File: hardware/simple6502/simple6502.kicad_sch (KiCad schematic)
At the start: 19 parts, among them J1 ~{VP}, J2 CLK SEL, J3 RESET, SW1 RESET, T1 DS1813-10+, U1 W65C02SxP, U2 RAM 62256, U3 ROM 28C256, U4 74LS30, U5 74HCT00, U6 74HC138, X1 ACO-1MHz

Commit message: All in One PCB  v1.1
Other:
- title: simple6502 -> All in One - simple6502
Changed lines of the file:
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@@
   (paper "USLetter")
   (title_block
-    (title "simple6502")
+    (title "All in One - simple6502")
     (date "2023-10-01")
     (rev "1.1")

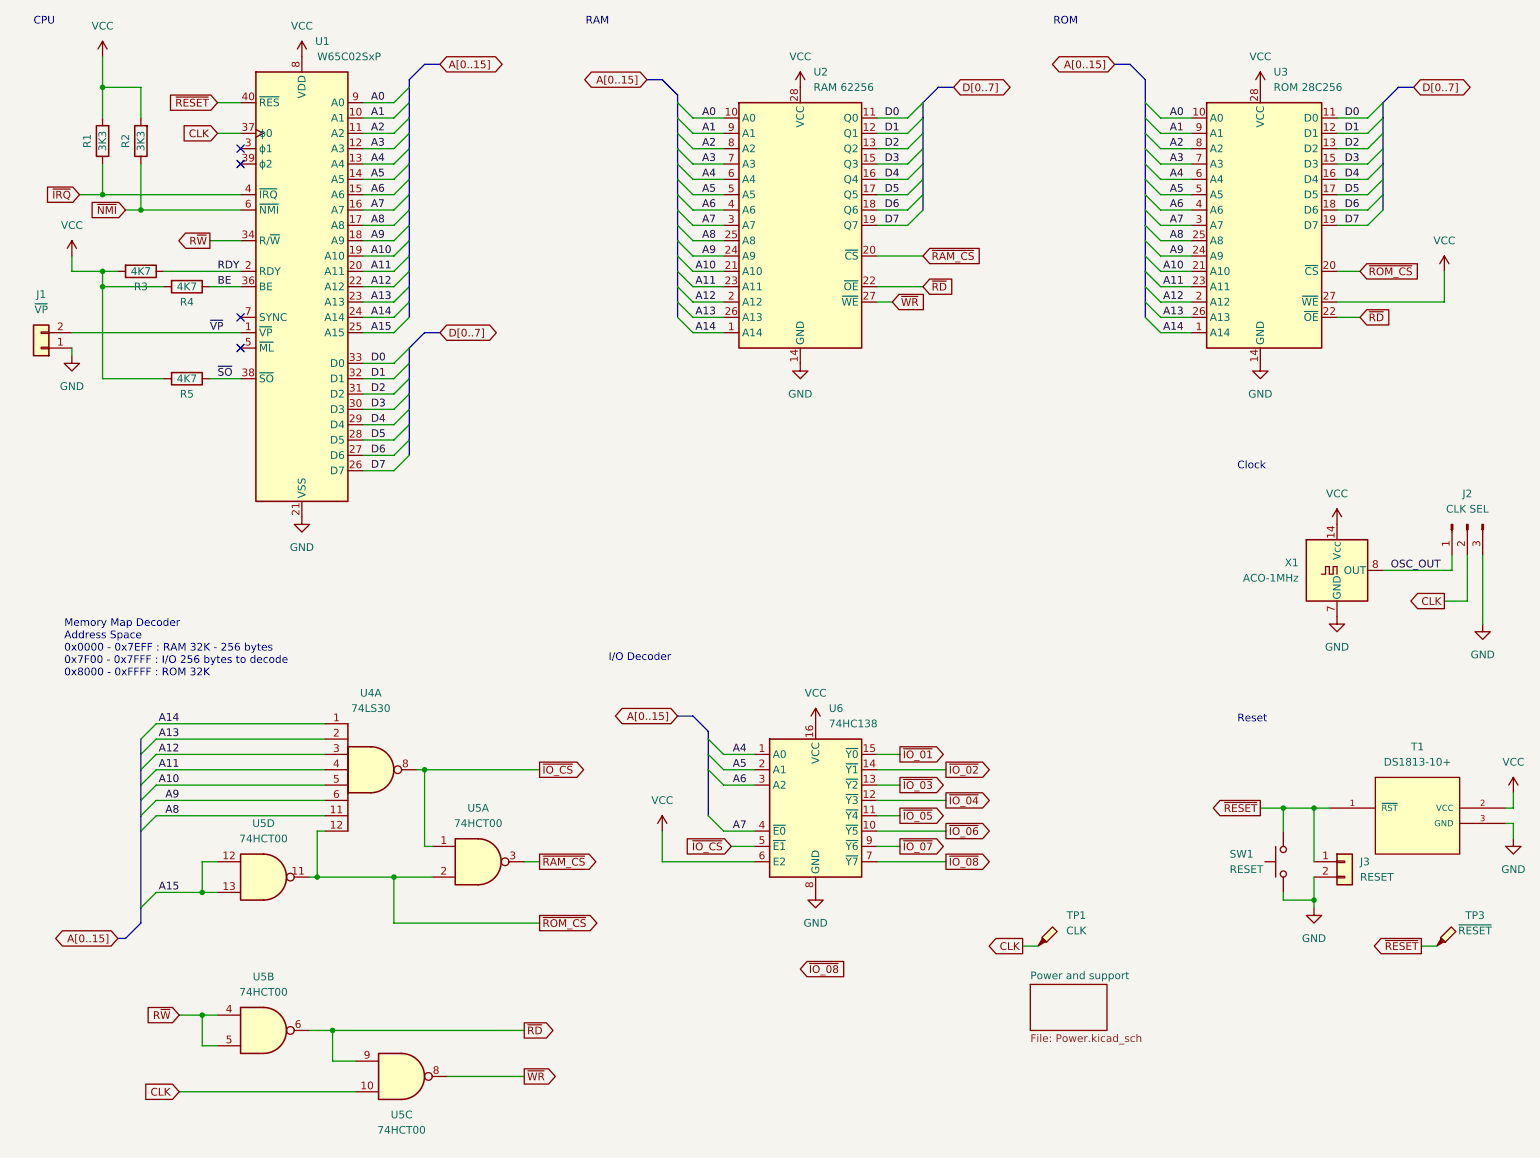
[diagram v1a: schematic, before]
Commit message: new all in one design with ACIA 68B50
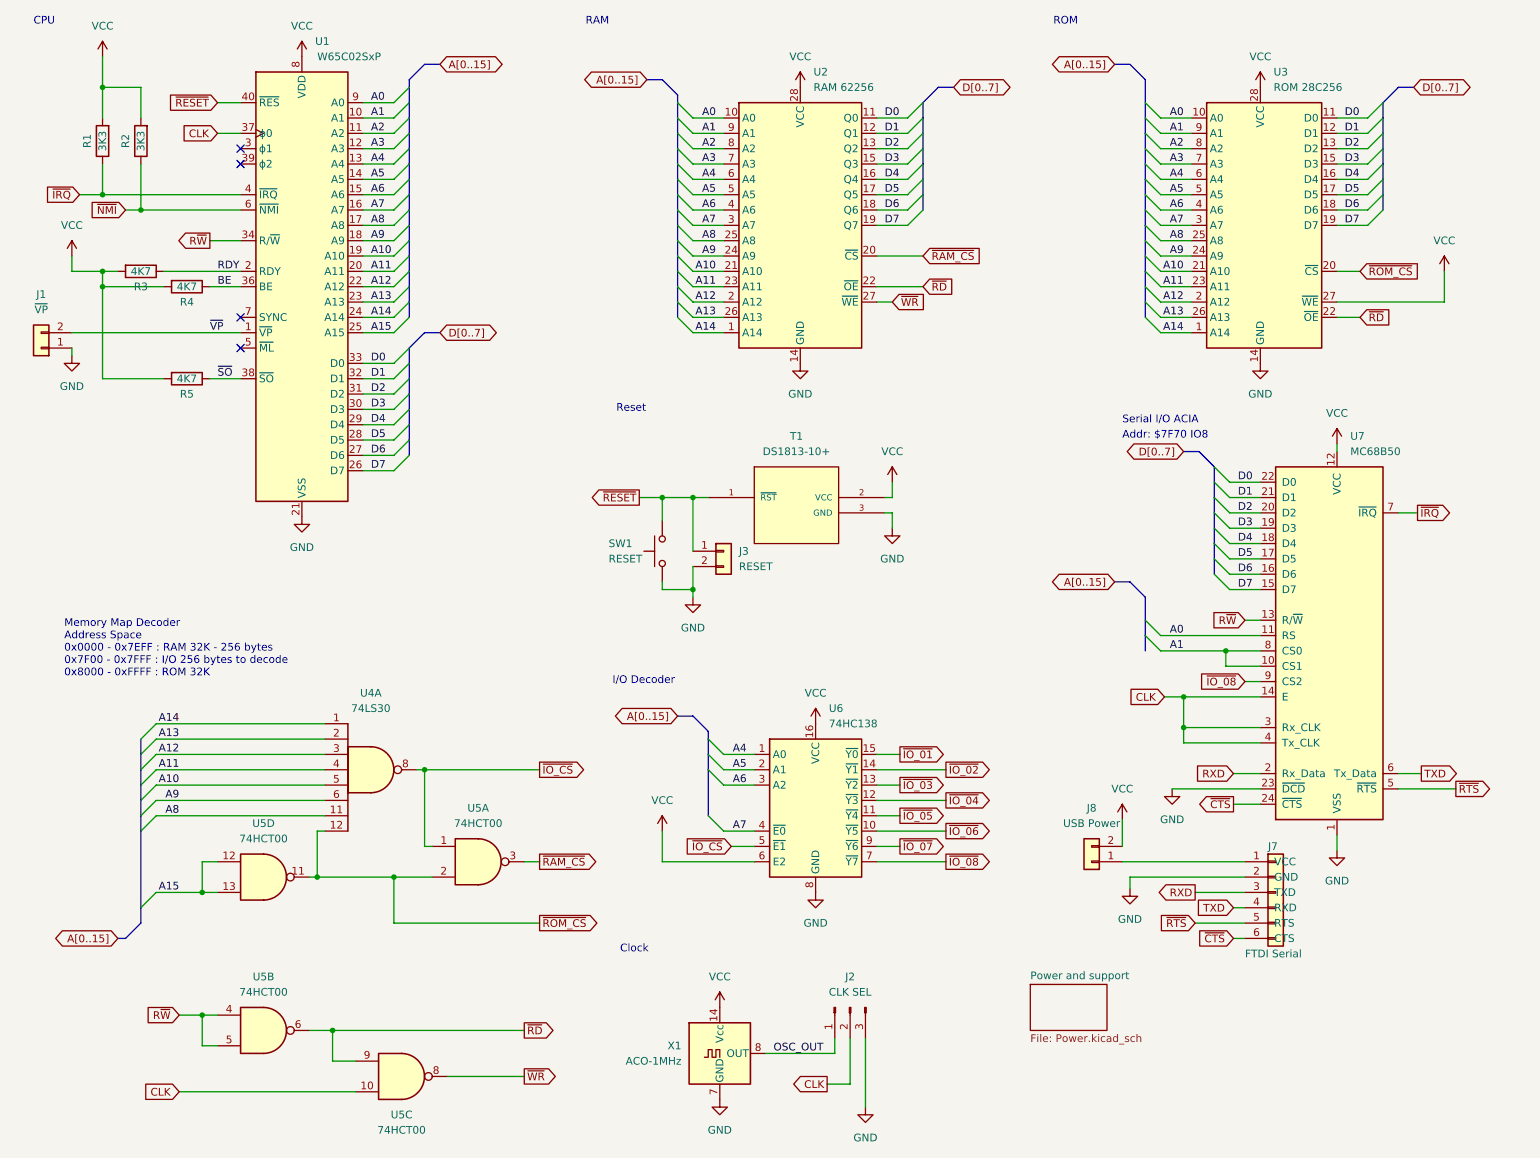
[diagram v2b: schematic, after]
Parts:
- removed TP1: CLK, TestPoint:TestPoint_THTPad_2.0x2.0mm_Drill1.0mm, symbol Connector:TestPoint_Probe
- removed TP3: ~{RESET}, TestPoint:TestPoint_THTPad_1.5x1.5mm_Drill0.7mm, symbol Connector:TestPoint_Probe
- added J7: FTDI Serial, Connector_PinSocket_2.54mm:PinSocket_1x06_P2.54mm_Vertical, symbol Connector_Generic:Conn_01x06
- added J8: USB Power, Connector_PinHeader_2.54mm:PinHeader_1x02_P2.54mm_Vertical, symbol Connector_Generic:Conn_01x02
- added U7: MC68B50, Package_DIP:DIP-24_W15.24mm_Socket, symbol Interface_UART:MC68B50
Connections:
- net A0: now also U7.11 (RS)
- net A1: now also U7.10 (CS1), U7.8 (CS0)
- net CLK: now also U7.14 (E), U7.3 (Rx_CLK), U7.4 (Tx_CLK)
- net D0: now also U7.22 (D0)
- net D1: now also U7.21 (D1)
- net D2: now also U7.20 (D2)
- net D3: now also U7.19 (D3)
- net D4: now also U7.18 (D4)
- net D5: now also U7.17 (D5)
- net D6: now also U7.16 (D6)
- net D7: now also U7.15 (D7)
- net GND: now also J7.2 (GND), U7.1 (VSS), U7.23 (~{DCD})
- net R~{W}: now also U7.13 (R/~{W})
- net VCC: now also J8.2 (Pin_2), U7.12 (VCC)
- net ~{IO_08}: now also U7.9 (CS2)
- net ~{IRQ}: now also U7.7 (~{IRQ})
- new net: J7.1 (VCC), J8.1 (Pin_1)
- new net RXD: J7.3 (TXD), U7.2 (Rx_Data)
- new net TXD: J7.4 (RXD), U7.6 (Tx_Data)
- new net ~{CTS}: J7.6 (CTS), U7.24 (~{CTS})
- new net ~{RTS}: J7.5 (RTS), U7.5 (~{RTS})
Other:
- note added: "Addr: $7F70 IO8"
- note added: "Serial I/O ACIA"
- moved on the sheet: J2, J3, SW1, T1, X1

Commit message: add the 40 pin header
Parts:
- J1: footprint Connector_PinHeader_2.54mm:PinHeader_1x02_P2.54mm_Vertical -> Jumper:SolderJumper-2_P1.3mm_Open_RoundedPad1.0x1.5mm
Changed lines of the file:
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@@
       (effects (font (size 1.27 1.27)))
     )
-    (property "Footprint" "Connector_PinHeader_2.54mm:PinHeader_1x02_P2.54mm_Vertical" (at 16.51 69.85 0)
+    (property "Footprint" "Jumper:SolderJumper-2_P1.3mm_Open_RoundedPad1.0x1.5mm" (at 16.51 69.85 0)
       (effects (font (size 1.27 1.27)) hide)
     )

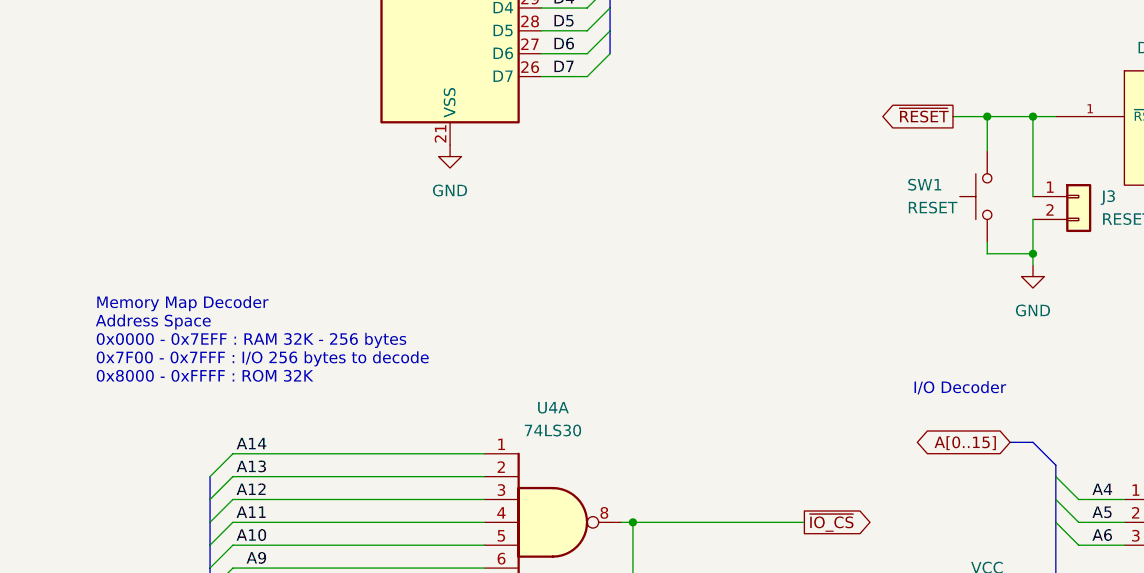
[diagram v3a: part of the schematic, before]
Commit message: port wired, new slot pinout
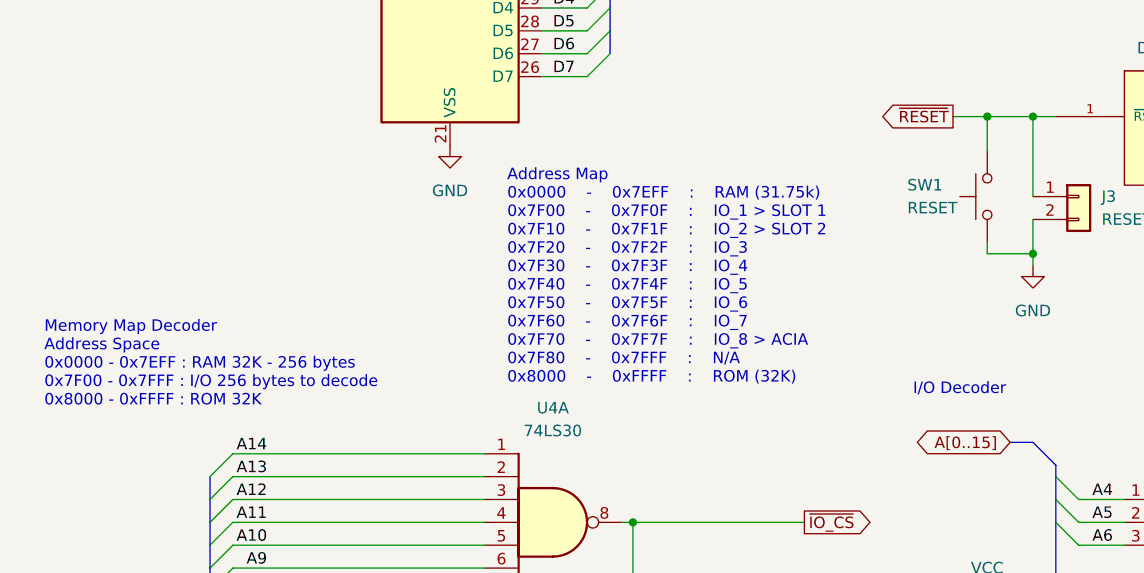
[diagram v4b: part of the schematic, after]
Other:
- note added: "Address Map 0x0000 - 0x7EFF : RAM (31.75k) 0x7F00 - 0x7F0F : IO_1 > SLOT 1 0x7F10 - 0x7F1F : IO_2 > SLOT 2 0x7F20 - 0x7F2F : IO_3 0x7F30 - 0x7F3F : IO_4 0x7F40 - 0x7F4F : IO_5 0x7F50 - 0x7F5F : IO_6 0x7F60 - 0x7F6F : IO_7 0x7F70 - 0x7F7F : IO_8 > ACIA 0x7F80 - 0x7FFF : N/A 0x8000 - 0xFFFF : ROM (32K)"
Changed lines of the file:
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@@
   )
   (text "Memory Map Decoder\nAddress Space\n0x0000 - 0x7EFF : RAM 32K - 256 bytes\n0x7F00 - 0x7FFF : I/O 256 bytes to decode\n0x8000 - 0xFFFF : ROM 32K\n"
-    (at 20.32 124.46 0)
+    (at 14.605 127 0)
     (effects (font (size 1.27 1.27)) (justify left bottom))
   )
@@
     (effects (font (size 1.27 1.27)) (justify left bottom))
   )
+  (text "Address Map				\n0x0000	-	0x7EFF	:	RAM (31.75k)\n0x7F00	-	0x7F0F	:	IO_1 > SLOT 1\n0x7F10	-	0x7F1F	:	IO_2 > SLOT 2\n0x7F20	-	0x7F2F	:	IO_3\n0x7F30	-	0x7F3F	:	IO_4\n0x7F40	-	0x7F4F	:	IO_5\n0x7F50	-	0x7F5F	:	IO_6\n0x7F60	-	0x7F6F	:	IO_7\n0x7F70	-	0x7F7F	:	IO_8 > ACIA\n0x7F80	-	0x7FFF	:	N/A\n0x8000	-	0xFFFF	:	ROM (32K)"
+    (at 66.04 124.46 0)
+    (effects (font (size 1.27 1.27)) (justify left bottom))
+  )
